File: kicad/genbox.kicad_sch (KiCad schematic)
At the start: 55 parts, among them J1 USB_A, SW15 SW_SPST, SW16 SW_SPST, SW17 SW_SPST, SW18 SW_SPST, U1 DM-OLED096-636, U2 rp2040-zero, U3 SN74LV1T34DBV

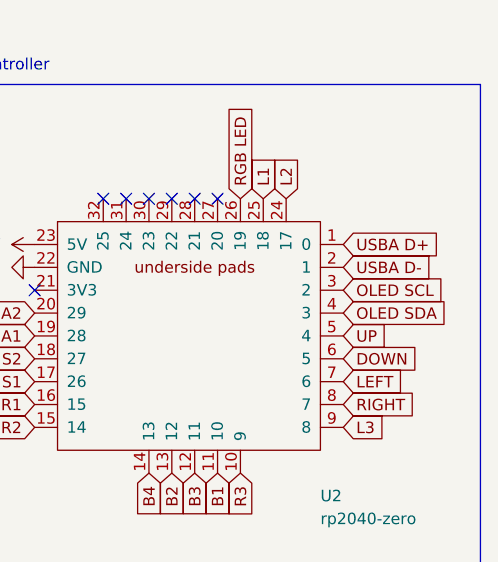
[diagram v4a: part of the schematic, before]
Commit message: usb a connection switch
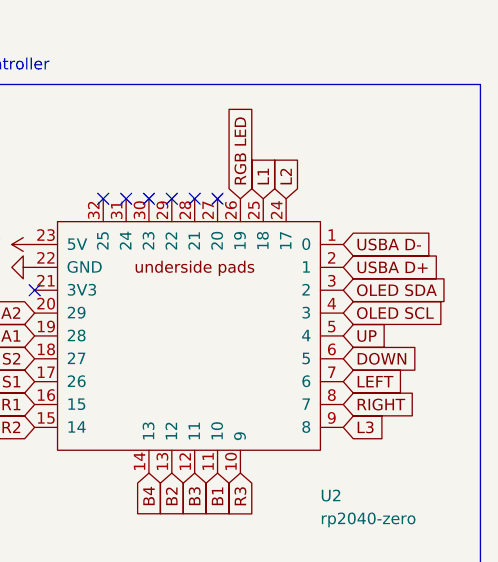
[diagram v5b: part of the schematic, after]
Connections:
- net OLED SCL: now also U2.4 (3); no longer U2.3 (2)
- net OLED SDA: now also U2.3 (2); no longer U2.4 (3)
- net USBA D+: now also U2.2 (1); no longer U2.1 (0)
- net USBA D-: now also U2.1 (0); no longer U2.2 (1)
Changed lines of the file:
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@@
     )
   )
-  (global_label "USBA D+" (shape input) (at 264.16 40.64 0) (fields_autoplaced)
+  (global_label "USBA D+" (shape input) (at 264.16 43.18 0) (fields_autoplaced)
     (effects (font (size 1.27 1.27)) (justify left))
-    (property "Intersheetrefs" "${INTERSHEET_REFS}" (at 275.8538 40.64 0)
+    (property "Intersheetrefs" "${INTERSHEET_REFS}" (at 275.8538 43.18 0)
       (effects (font (size 1.27 1.27)) (justify left) hide)
     )
@@
     )
   )
-  (global_label "OLED SCL" (shape input) (at 264.16 45.72 0) (fields_autoplaced)
+  (global_label "OLED SCL" (shape input) (at 264.16 48.26 0) (fields_autoplaced)
     (effects (font (size 1.27 1.27)) (justify left))
-    (property "Intersheetrefs" "${INTERSHEET_REFS}" (at 276.398 45.72 0)
+    (property "Intersheetrefs" "${INTERSHEET_REFS}" (at 276.398 48.26 0)
       (effects (font (size 1.27 1.27)) (justify left) hide)
     )
@@
     )
   )
-  (global_label "OLED SDA" (shape input) (at 264.16 48.26 0) (fields_autoplaced)
+  (global_label "OLED SDA" (shape input) (at 264.16 45.72 0) (fields_autoplaced)
     (effects (font (size 1.27 1.27)) (justify left))
-    (property "Intersheetrefs" "${INTERSHEET_REFS}" (at 276.4585 48.26 0)
+    (property "Intersheetrefs" "${INTERSHEET_REFS}" (at 276.4585 45.72 0)
       (effects (font (size 1.27 1.27)) (justify left) hide)
     )
@@
     )
   )
-  (global_label "USBA D-" (shape input) (at 264.16 43.18 0) (fields_autoplaced)
+  (global_label "USBA D-" (shape input) (at 264.16 40.64 0) (fields_autoplaced)
     (effects (font (size 1.27 1.27)) (justify left))
-    (property "Intersheetrefs" "${INTERSHEET_REFS}" (at 275.8538 43.18 0)
+    (property "Intersheetrefs" "${INTERSHEET_REFS}" (at 275.8538 40.64 0)
       (effects (font (size 1.27 1.27)) (justify left) hide)
     )
